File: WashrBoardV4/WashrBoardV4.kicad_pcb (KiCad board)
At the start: 2 copper layers, 70 x 50 mm, 37 parts, among them J1 TestPoint 5V, J10 ProgPoint GND, J2 USB_C_Receptacle_USB2.0_16P, J3 TestPoint GND, J4 TestPoint 3.3V, J5 JST GH, J6 ProgPoint 5V, J7 ProgPoint P9 GND, J8 ProgPointPoint D_P, J9 ProgPoint D_N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

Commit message: Initial routing
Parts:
- turned C2 to 180 degrees
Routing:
- net GND: track 0.00 -> 174.7 mm, vias 0 -> 10
- net +3.3V: track 0.00 -> 173.9 mm, vias 0 -> 2
- net VBUS: track 2.75 -> 53.7 mm, vias 1 -> 3
- net Net-(U4-IO9): track 0.00 -> 47.3 mm, vias 0 -> 3
- net Net-(U4-IO10): track 0.00 -> 31.4 mm, vias 0 -> 2
- net Net-(U4-IO6): track 0.00 -> 27.6 mm, vias 0 -> 2
- net Net-(J2-CC2): track 0.00 -> 25.4 mm, vias 0 -> 2
- net /SCL: track 0.00 -> 25.3 mm, vias 0 -> 2
- net Net-(J2-CC1): track 0.00 -> 23.6 mm, vias 0 -> 2
- net /SDA: track 0.00 -> 21.0 mm, vias 0 -> 2
- net Net-(U4-EN): track 0.00 -> 20.5 mm, vias 0 -> 2
- net Net-(U4-IO8): track 0.00 -> 13.6 mm, vias 0 -> 2
- net Net-(U4-IO2): track 0.00 -> 11.3 mm
- net Net-(D2-A): track 0.00 -> 9.87 mm
- net Net-(D1-A): track 0.00 -> 9.26 mm

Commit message: Finished routing of V4
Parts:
- J10, J6, J7, J8, J9: moved to B.Cu
- moved J6 41.3 mm to (168.5, 73.0), turned to -90 degrees
- moved J8 37.0 mm to (168.5, 75.5), turned to -90 degrees
- moved J9 29.3 mm to (168.5, 78.0), turned to -90 degrees
- moved J10 28.5 mm to (168.5, 83.0), turned to -90 degrees
- moved J7 18.2 mm to (168.5, 80.5), turned to -90 degrees
- moved R4 6.00 mm to (160.0, 77.0)
- moved R6 6.00 mm to (150.0, 77.0)
- moved D1 4.50 mm to (160.0, 82.5)
- moved D2 4.50 mm to (150.0, 82.5)
- turned C3 to 180 degrees
- turned C4 to 0 degrees
- turned C6 to 180 degrees
- turned R10 to 180 degrees
- turned R7 to 180 degrees
- turned R8 to 180 degrees
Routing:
- net GND: track 174.7 -> 241.9 mm, vias 10 -> 13
- net VBUS: track 53.7 -> 106.7 mm, vias 3 -> 5
- net /D_P: track 10.9 -> 62.4 mm, vias 0 -> 1
- net /D_N: track 12.8 -> 56.4 mm, vias 0 -> 1
- net /ProgGND: track 0.00 -> 15.3 mm, vias 0 -> 1
- net Net-(U4-EN): track 20.5 -> 13.7 mm, vias 2 -> 0
- net +3.3V: track 173.9 -> 180.1 mm, vias 2 -> 6
- net Net-(U4-IO6): track 27.6 -> 22.7 mm
- net Net-(U4-IO8): track 13.6 -> 9.52 mm, vias 2 -> 0
- net /SCL: track 25.3 -> 22.6 mm
- net Net-(J2-CC1): track 23.6 -> 25.6 mm
- net Net-(J2-CC2): track 25.4 -> 27.1 mm
- net Net-(D2-A): track 9.87 -> 11.4 mm
- net Net-(D1-A): track 9.26 -> 10.1 mm
- net Net-(U4-IO9): track 47.3 -> 46.6 mm

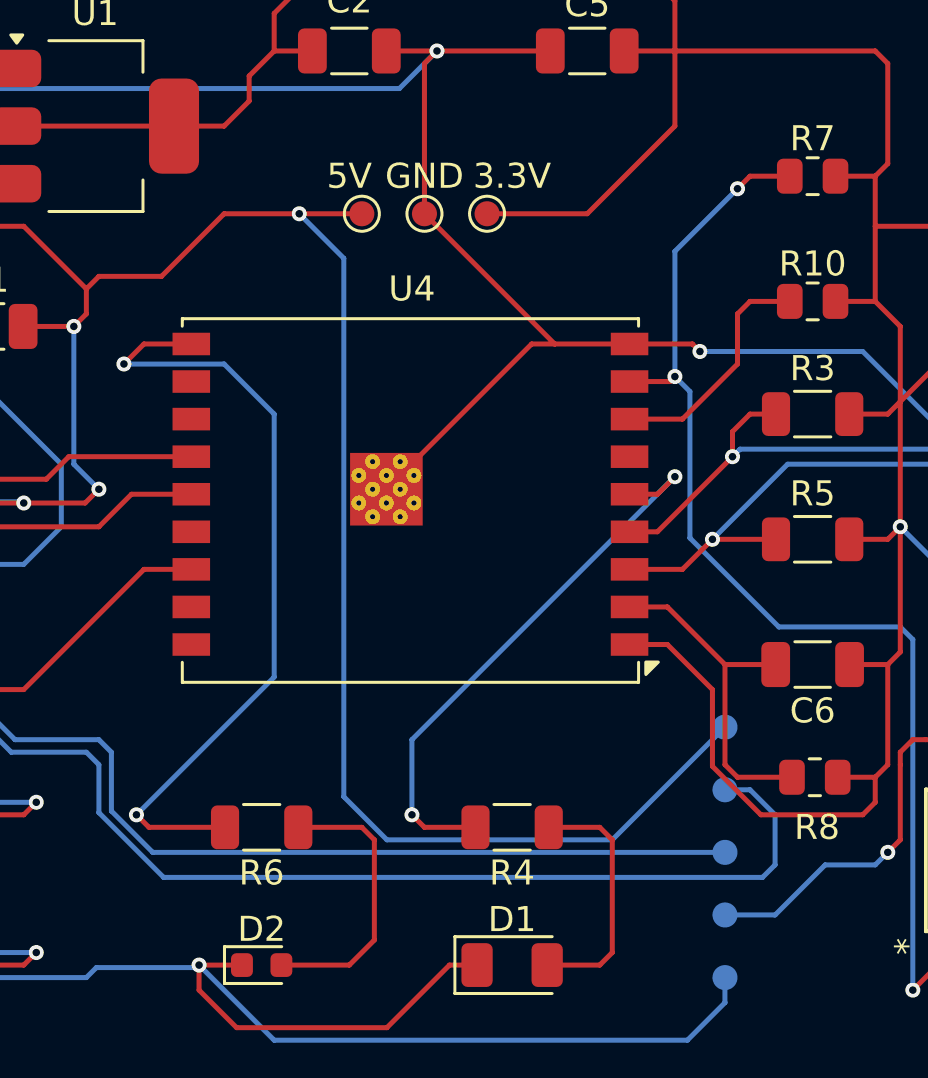
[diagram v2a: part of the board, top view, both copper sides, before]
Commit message: Adjusted testpoint pad spacing
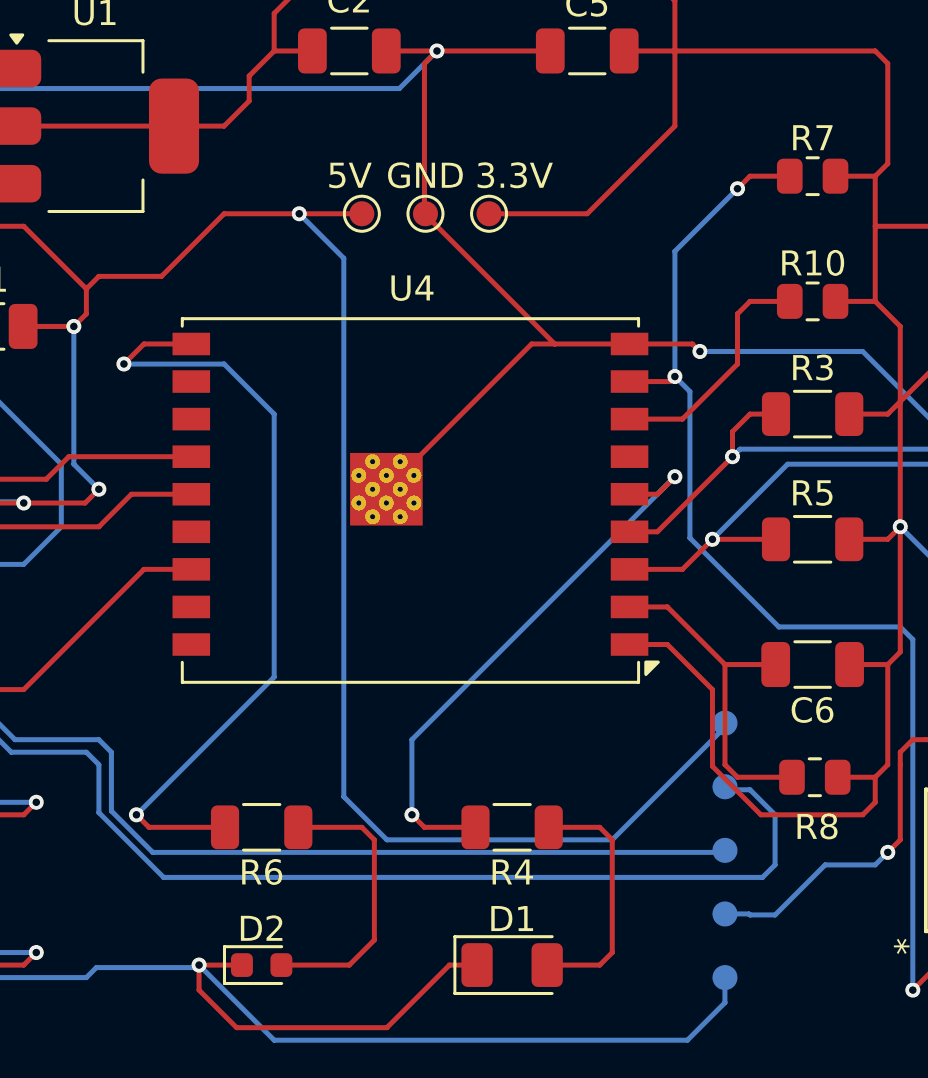
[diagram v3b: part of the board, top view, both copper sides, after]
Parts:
- moved J6 0.16 mm to (168.5, 72.8)
- moved J8 0.12 mm to (168.5, 75.4)
- moved J4 0.08 mm to (159.1, 52.5)
- moved J9 0.08 mm to (168.5, 77.9)
